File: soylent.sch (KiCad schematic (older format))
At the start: 24 parts, among them J1 DB9_Female, J2 Conn_01x04, J3 Conn_01x04, J4 Conn_02x03_Counter_Clockwise, Q1 BC847BPN, Q2 BC847BPN, U1 ATtiny202-SS, U2 MIC5504-3.3YM5

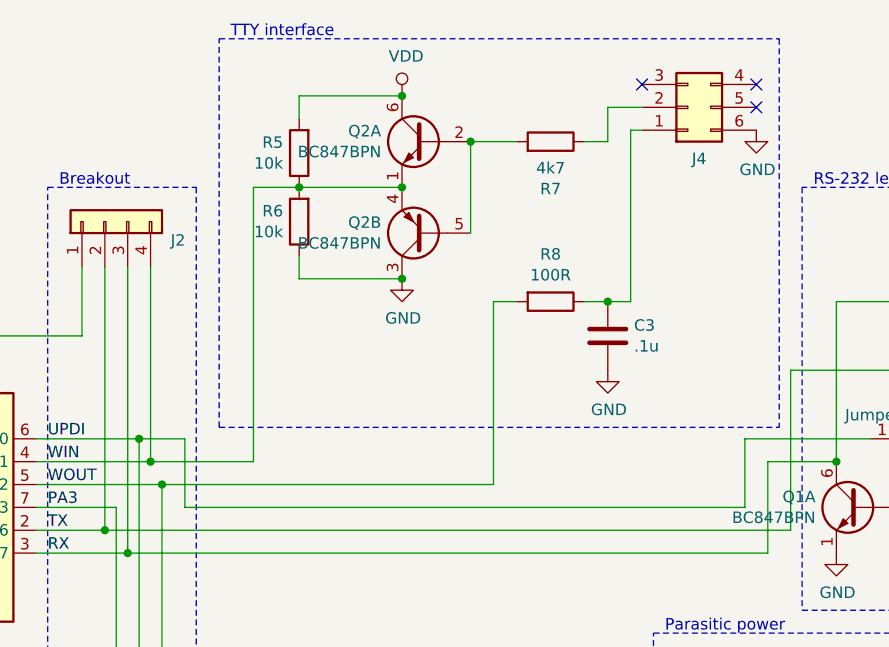
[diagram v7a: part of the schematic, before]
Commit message: Add a transistor to simulate mic
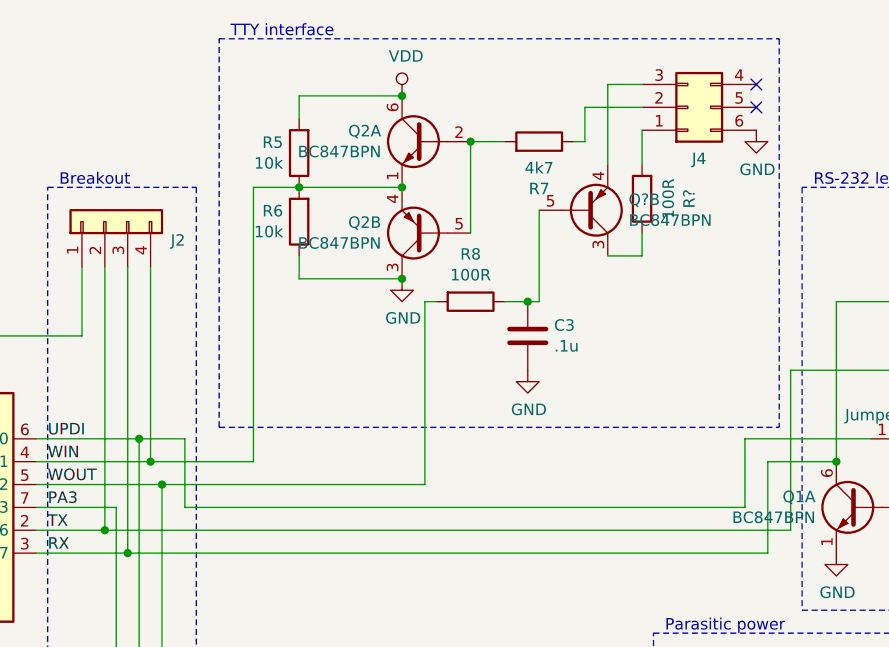
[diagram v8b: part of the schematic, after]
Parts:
- added Q?: BC847BPN, TO_SOT_Packages_SMD:SOT-363_SC-70-6_Handsoldering, symbol Transistor_BJT:BC847BPN
- added R?: 100R, Resistors_SMD:R_0603_HandSoldering, symbol Device:R
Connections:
- net at C3.1, R8.1: now also Q?.5 (B2); no longer J4.1 (Pin_1)
- net at J4.3 (Pin_3): now also Q?.4 (E2)
- new net: J4.1 (Pin_1), R?.2
- new net: Q?.3 (C2), R?.1
- no-connect marks 7 -> 6
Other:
- moved on the sheet: C3, R7, R8
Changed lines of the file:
@@
-$EndComp
-$Comp
-L Device:R R7
-U 1 1 5DEFDFE7
-P 5700 2200
-F 0 "R7" V 5493 2200 50  0000 C CNN
-F 1 "4k7" V 5584 2200 50  0000 C CNN
-F 2 "Resistors_SMD:R_0603_HandSoldering" V 5630 2200 50  0001 C CNN
-F 3 "~" H 5700 2200 50  0001 C CNN
-	1    5700 2200
-	0    1    -1   0
 $EndComp
 $Comp
@@
 Wire Wire Line
 	5350 2600 5350 2200
-Wire Wire Line
-	5350 2200 5550 2200
 Connection ~ 5350 2200
 $Comp
@@
 Wire Wire Line
 	4400 2400 4600 2400
-NoConn ~ 6100 1950
 NoConn ~ 6600 1950
 NoConn ~ 6600 2050
@@
 L Device:R R8
 U 1 1 5DFD8224
-P 5700 2900
-F 0 "R8" V 5493 2900 50  0000 C CNN
-F 1 "100R" V 5584 2900 50  0000 C CNN
-F 2 "Resistors_SMD:R_0603_HandSoldering" V 5630 2900 50  0001 C CNN
-F 3 "~" H 5700 2900 50  0001 C CNN
-	1    5700 2900
+P 5350 2900
+F 0 "R8" V 5143 2900 50  0000 C CNN
+F 1 "100R" V 5234 2900 50  0000 C CNN
+F 2 "Resistors_SMD:R_0603_HandSoldering" V 5280 2900 50  0001 C CNN
+F 3 "~" H 5350 2900 50  0001 C CNN
+	1    5350 2900
 	0    1    1    0
 $EndComp
@@
 L Device:C C3
 U 1 1 5DFEE336
-P 5950 3050
-F 0 "C3" H 6065 3096 50  0000 L CNN
-F 1 ".1u" H 6065 3005 50  0000 L CNN
-F 2 "Capacitor_SMD:C_0603_1608Metric_Pad1.05x0.95mm_HandSolder" H 5988 2900 50  0001 C CNN
-F 3 "~" H 5950 3050 50  0001 C CNN
-	1    5950 3050
+P 5600 3050
+F 0 "C3" H 5715 3096 50  0000 L CNN
+F 1 ".1u" H 5715 3005 50  0000 L CNN
+F 2 "Capacitor_SMD:C_0603_1608Metric_Pad1.05x0.95mm_HandSolder" H 5638 2900 50  0001 C CNN
+F 3 "~" H 5600 3050 50  0001 C CNN
+	1    5600 3050
 	1    0    0    -1
 $EndComp
@@
 L power:GND #PWR0111
 U 1 1 5DFEEE43
-P 5950 3200
-F 0 "#PWR0111" H 5950 2950 50  0001 C CNN
-F 1 "GND" H 5955 3027 50  0000 C CNN
-F 2 "" H 5950 3200 50  0001 C CNN
-F 3 "" H 5950 3200 50  0001 C CNN
-	1    5950 3200
-	1    0    0    -1
-$EndComp
-Wire Wire Line
-	5850 2900 5950 2900
+P 5600 3200
+F 0 "#PWR0111" H 5600 2950 50  0001 C CNN
+F 1 "GND" H 5605 3027 50  0000 C CNN
+F 2 "" H 5600 3200 50  0001 C CNN
+F 3 "" H 5600 3200 50  0001 C CNN
+	1    5600 3200
+	1    0    0    -1
+$EndComp
+Wire Wire Line
+	5500 2900 5600 2900
 Wire Wire Line
 	7500 3500 7650 3500
@@
 	7650 3600 7650 3800
 Wire Wire Line
-	5850 2200 5950 2200
-Wire Wire Line
-	5950 2200 5950 2050
-Wire Wire Line
-	5950 2050 6100 2050
+	5800 2200 5850 2200
+Wire Wire Line
+	5850 2200 5850 2050
+Wire Wire Line
+	5850 2050 6100 2050
 Wire Wire Line
 	4400 2400 4400 3600
-Wire Wire Line
-	5950 2900 6050 2900
-Wire Wire Line
-	6050 2900 6050 2150
-Wire Wire Line
-	6050 2150 6100 2150
-Connection ~ 5950 2900
 Connection ~ 5050 2800
 $Comp
@@
 $EndComp
 Wire Wire Line
-	5450 2900 5550 2900
-Wire Wire Line
-	4000 3700 5450 3700
-Wire Wire Line
-	5450 3700 5450 2900
+	4000 3700 5150 3700
+Wire Wire Line
+	5150 3700 5150 2900
+Wire Wire Line
+	6100 1950 5950 1950
+Wire Wire Line
+	5950 1950 5950 2300
+Wire Wire Line
+	5150 2900 5200 2900
+Wire Wire Line
+	5350 2200 5500 2200
+$Comp
+L Device:R R7
+U 1 1 5DEFDFE7
+P 5650 2200
+F 0 "R7" V 5443 2200 50  0000 C CNN
+F 1 "4k7" V 5534 2200 50  0000 C CNN
+F 2 "Resistors_SMD:R_0603_HandSoldering" V 5580 2200 50  0001 C CNN
+F 3 "~" H 5650 2200 50  0001 C CNN
+	1    5650 2200
+	0    1    -1   0
+$EndComp
+$Comp
+L Transistor_BJT:BC847BPN Q?
+U 2 1 5E1133DF
+P 5850 2500
+F 0 "Q?" H 6041 2454 50  0000 L CNN
+F 1 "BC847BPN" H 6041 2545 50  0000 L CNN
+F 2 "TO_SOT_Packages_SMD:SOT-363_SC-70-6_Handsoldering" H 6050 2600 50  0001 C CNN
+F 3 "https://assets.nexperia.com/documents/data-sheet/BC847BPN.pdf" H 5850 2500 50  0001 C CNN
+	2    5850 2500
+	1    0    0    1
+$EndComp
+Wire Wire Line
+	5600 2900 5650 2900
+Wire Wire Line
+	5650 2900 5650 2500
+Connection ~ 5600 2900
+Wire Wire Line
+	5950 2700 6100 2700
+Wire Wire Line
+	6100 2700 6100 2600
+$Comp
+L Device:R R?
+U 1 1 5E15CC34
+P 6100 2450
+F 0 "R?" V 5893 2450 50  0000 C CNN
+F 1 "100R" V 5984 2450 50  0000 C CNN
+F 2 "Resistors_SMD:R_0603_HandSoldering" V 6030 2450 50  0001 C CNN
+F 3 "~" H 6100 2450 50  0001 C CNN
+	1    6100 2450
+	-1   0    0    1
+$EndComp
+Wire Wire Line
+	6100 2300 6100 2150
 $EndSCHEMATC
